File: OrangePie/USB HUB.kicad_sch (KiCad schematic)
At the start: 0 parts

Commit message: Add usb hub and can tranceiver
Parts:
- added C16, C8: 10uF, PCM_JLCPCB:C_0402, symbol PCM_JLCPCB-Capacitors:0402,10uF
- added C17: 100nF, PCM_JLCPCB:C_0402, symbol PCM_JLCPCB-Capacitors:0402,100nF
- added C7: 1uF, PCM_JLCPCB:C_0402, symbol PCM_JLCPCB-Capacitors:0402,1uF
- added U3: CH334R, Package_SO:QSOP-16_3.9x4.9mm_P0.635mm, symbol WCH_USB:CH334R
- added Y1: 12MHz, Crystal:Crystal_SMD_3225-4Pin_3.2x2.5mm, symbol Device:Crystal_GND24_Small
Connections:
- new net: U3.16 (XI), Y1.1
- new net: U3.15 (XO), Y1.3
- new net: C7.1, C8.1, U3.13 (VDD33)
- new net +5V: C16.1, C17.1, U3.12 (V5)
- new net GND: C16.2, C17.2, C7.2, C8.2, U3.14 (GND), Y1.2, Y1.4
- new net USB3.+: U3.6 (DP2)
- new net USB3.-: U3.5 (DM2)
- new net USB4.+: U3.8 (DP1)
- new net USB4.-: U3.7 (DM1)
- new net USB_AUDIO.+: U3.2 (DP4)
- new net USB_AUDIO.-: U3.1 (DM4)
- new net USB_CAN.+: U3.4 (DP3)
- new net USB_CAN.-: U3.3 (DM3)
- new net USB_SBC.+: U3.11 (DPU)
- new net USB_SBC.-: U3.10 (DMU)
- no-connect marks 0 -> 1
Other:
- note added: "HUB IC"

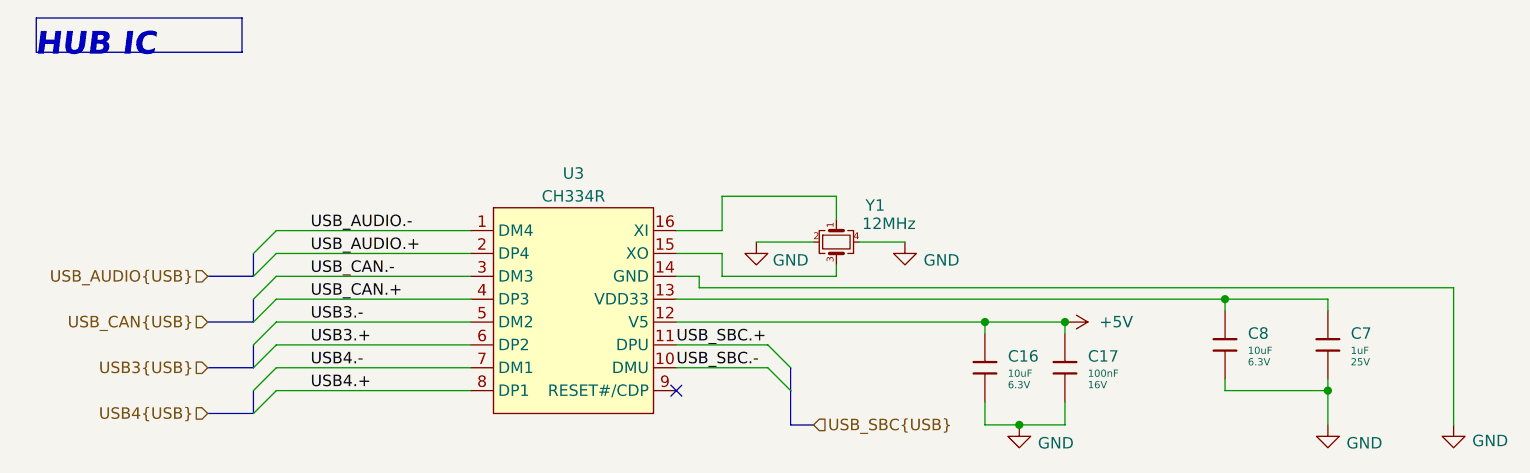
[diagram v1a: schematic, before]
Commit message: Update rest of schematic
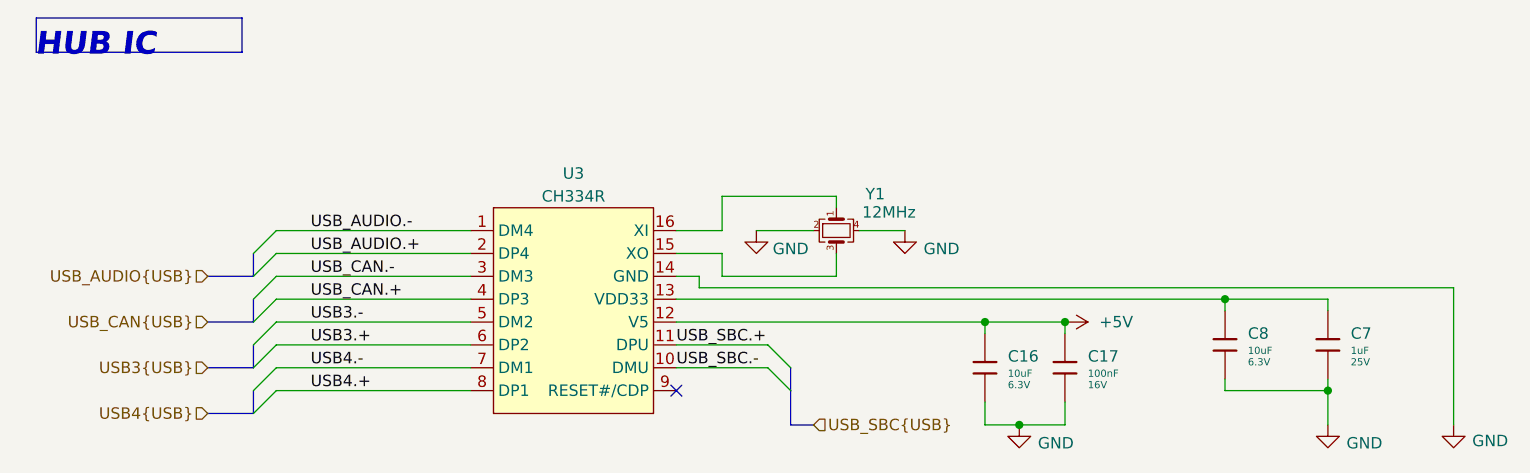
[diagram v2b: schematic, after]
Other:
- moved on the sheet: Y1
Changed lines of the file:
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@@
 	(wire
 		(pts
-			(xy 157.48 95.25) (xy 162.56 95.25)
+			(xy 157.48 93.98) (xy 162.56 93.98)
 		)
 		(stroke
@@
 	(wire
 		(pts
-			(xy 152.4 95.25) (xy 146.05 95.25)
+			(xy 152.4 93.98) (xy 146.05 93.98)
 		)
 		(stroke
@@
 	(wire
 		(pts
-			(xy 154.94 97.79) (xy 154.94 99.06)
-		)
-		(stroke
-			(width 0)
-			(type default)
-		)
-	)
-	(wire
-		(pts
-			(xy 154.94 92.71) (xy 154.94 90.17)
+			(xy 154.94 96.52) (xy 154.94 99.06)
+		)
+		(stroke
+			(width 0)
+			(type default)
+		)
+	)
+	(wire
+		(pts
+			(xy 154.94 91.44) (xy 154.94 90.17)
 		)
 		(stroke
@@
 	(symbol
 		(lib_id "Device:Crystal_GND24_Small")
-		(at 154.94 95.25 270)
+		(at 154.94 93.98 270)
 		(unit 1)
 		(exclude_from_sim no)
@@
 		(dnp no)
 		(property "Reference" "Y1"
-			(at 159.258 91.186 90)
+			(at 159.258 89.916 90)
 			(effects
 				(font
@@
 		)
 		(property "Value" "12MHz"
-			(at 160.782 93.218 90)
+			(at 160.782 91.948 90)
 			(effects
 				(font
@@
 		)
 		(property "Footprint" "Crystal:Crystal_SMD_3225-4Pin_3.2x2.5mm"
-			(at 154.94 95.25 0)
+			(at 154.94 93.98 0)
 			(effects
 				(font
@@
 		)
 		(property "Datasheet" "~"
-			(at 154.94 95.25 0)
+			(at 154.94 93.98 0)
 			(effects
 				(font
@@
 		)
 		(property "Description" ""
-			(at 154.94 95.25 0)
+			(at 154.94 93.98 0)
 			(effects
 				(font
@@
 		(lib_name "GND_1")
 		(lib_id "power:GND")
-		(at 146.05 95.25 0)
+		(at 146.05 93.98 0)
 		(unit 1)
 		(exclude_from_sim no)
@@
 		(dnp no)
 		(property "Reference" "#PWR010"
-			(at 146.05 101.6 0)
+			(at 146.05 100.33 0)
 			(effects
 				(font
@@
 		)
 		(property "Value" "GND"
-			(at 149.86 97.282 0)
+			(at 149.86 96.012 0)
 			(effects
 				(font
@@
 		)
 		(property "Footprint" ""
-			(at 146.05 95.25 0)
+			(at 146.05 93.98 0)
 			(effects
 				(font
@@
 		)
 		(property "Datasheet" ""
-			(at 146.05 95.25 0)
+			(at 146.05 93.98 0)
 			(effects
 				(font
@@
 		)
 		(property "Description" "Power symbol creates a global label with name \"GND\" , ground"
-			(at 146.05 95.25 0)
+			(at 146.05 93.98 0)
 			(effects
 				(font
@@
 		(lib_name "GND_1")
 		(lib_id "power:GND")
-		(at 162.56 95.25 0)
+		(at 162.56 93.98 0)
 		(unit 1)
 		(exclude_from_sim no)
@@
 		(dnp no)
 		(property "Reference" "#PWR011"
-			(at 162.56 101.6 0)
+			(at 162.56 100.33 0)
 			(effects
 				(font
@@
 		)
 		(property "Value" "GND"
-			(at 166.624 97.282 0)
+			(at 166.624 96.012 0)
 			(effects
 				(font
@@
 		)
 		(property "Footprint" ""
-			(at 162.56 95.25 0)
+			(at 162.56 93.98 0)
 			(effects
 				(font
@@
 		)
 		(property "Datasheet" ""
-			(at 162.56 95.25 0)
+			(at 162.56 93.98 0)
 			(effects
 				(font
@@
 		)
 		(property "Description" "Power symbol creates a global label with name \"GND\" , ground"
-			(at 162.56 95.25 0)
-			(effects
-				(font
+			(at 162.56 93.98 0)
+			(effects
+				(font

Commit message: Add CH340 debug
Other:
- company: (none) -> ModuCard System
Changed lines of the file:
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@@
 	(generator_version "8.0")
 	(paper "A4")
+	(title_block
+		(date "2025-02-10")
+		(rev "A")
+		(company "ModuCard System")
+	)
 	(junction
 		(at 209.55 111.76)
@@
 	(label "USB_CAN.+"
 		(at 96.52 101.6 0)
+		(fields_autoplaced yes)
 		(effects
 			(font
@@
 	(label "USB3.+"
 		(at 96.52 106.68 0)
+		(fields_autoplaced yes)
 		(effects
 			(font
@@
 	(label "USB_SBC.+"
 		(at 137.16 106.68 0)
+		(fields_autoplaced yes)
 		(effects
 			(font
@@
 	(label "USB_SBC.-"
 		(at 137.16 109.22 0)
+		(fields_autoplaced yes)
 		(effects
 			(font
@@
 	(label "USB4.-"
 		(at 96.52 109.22 0)
+		(fields_autoplaced yes)
 		(effects
 			(font
@@
 	(label "USB_AUDIO.+"
 		(at 96.52 96.52 0)
+		(fields_autoplaced yes)
 		(effects
 			(font
@@
 	(label "USB_CAN.-"
 		(at 96.52 99.06 0)
+		(fields_autoplaced yes)
 		(effects
 			(font
@@
 	(label "USB3.-"
 		(at 96.52 104.14 0)
+		(fields_autoplaced yes)
 		(effects
 			(font
@@
 	(label "USB_AUDIO.-"
 		(at 96.52 93.98 0)
+		(fields_autoplaced yes)
 		(effects
 			(font
@@
 	(label "USB4.+"
 		(at 96.52 111.76 0)
-		(effects
-			(font
+		(fields_autoplaced yes)
+		(effects
+			(font
